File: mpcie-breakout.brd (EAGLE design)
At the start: 70 x 70 mm, 43 parts, among them K1 694108106102, U1 IP4234CZ6, U2 LD1085D2T33R, X1 MPCIE-JAE, X2 MINI-USB-SHIELD-UX60-MB-5ST

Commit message: gitflow-feature-stash: nanoSIM
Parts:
- removed SIM1: SF7W008S1A-R, SF7W008S1A-SIM:SF7W008S1A-RESTR
- removed X3, X4, X5: (no value), laforge:SMA-F-S-TH
- removed Y3, Y4, Y5: (no value), laforge:HRS_UFL
- added J1: 693043020611, Wurth_Connectors_WR-CRD:693043020611
- moved C8 20.9 mm to (-4.95, 47.1)
- moved C7 14.4 mm to (-13.0, 45.0)
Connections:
- removed net N$13: X3.C, Y3.SIG
- removed net N$14: X4.C, Y4.SIG
- removed net N$7: X5.C, Y5.SIG
- net GND: now also J1.C5, J1.S1, J1.S2, J1.S3, J1.S4, J1.S5, J1.S6; no longer SIM1.5, X3.G1, X3.G2, X3.G3, X3.G4, X4.G1, X4.G2, X4.G3, X4.G4, X5.G1, X5.G2, X5.G3, X5.G4, Y3.GND@1, Y3.GND@2, Y4.GND@1, Y4.GND@2, Y5.GND@1, Y5.GND@2
- net USIM_CLK: now also J1.C3; no longer SIM1.3
- net USIM_DATA: now also J1.C7; no longer SIM1.7
- net USIM_POWER: now also J1.C1; no longer SIM1.1
- net USIM_RESET: now also J1.C2; no longer SIM1.2
- net USIM_VPP: now also J1.C6; no longer SIM1.6
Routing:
- net USIM_VPP: track 34.2 -> 17.7 mm
- net USIM_DATA: track 25.1 -> 10.7 mm
- net USIM_POWER: track 35.2 -> 21.4 mm
- net N$14: track 5.61 -> 0.00 mm
- net N$13: track 5.61 -> 0.00 mm
- net N$7: track 5.36 -> 0.00 mm
- net USIM_RESET: track 36.1 -> 37.3 mm
- net USIM_CLK: track 31.5 -> 32.7 mm
- net GND: vias 164 -> 155

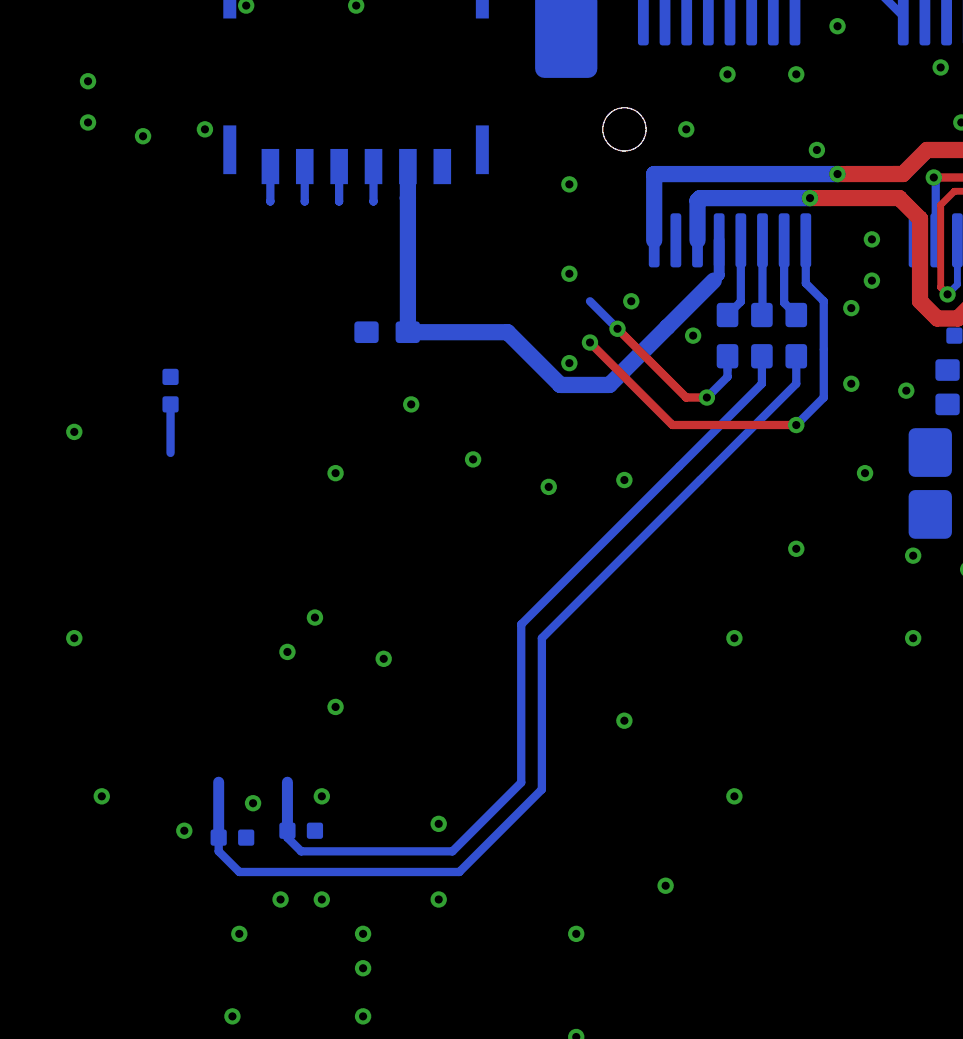
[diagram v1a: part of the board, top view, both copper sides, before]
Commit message: Nano Sim placed.
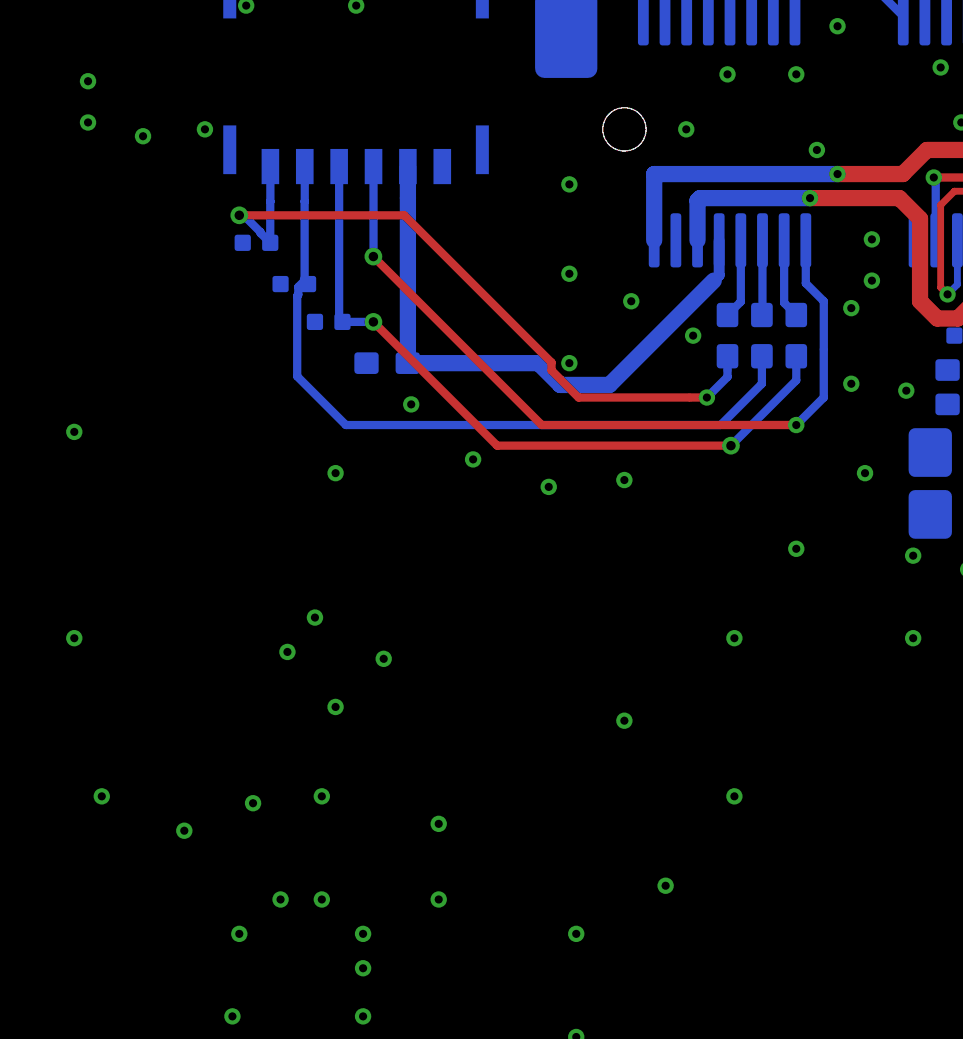
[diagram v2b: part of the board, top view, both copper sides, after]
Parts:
- moved C5 20.2 mm to (-8.38, 48.9), turned to 0 degrees
- moved C6 19.4 mm to (-7.11, 47.5), turned to 0 degrees
- moved C7 6.32 mm to (-9.78, 50.4), turned to 0 degrees
- moved C8 1.14 mm to (-4.95, 46.0)
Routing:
- net USIM_DATA: track 10.7 -> 26.5 mm
- net USIM_VPP: track 17.7 -> 29.0 mm
- net USIM_RESET: track 37.3 -> 26.3 mm, vias 0 -> 2
- net USIM_CLK: track 32.7 -> 27.6 mm
- net USIM_POWER: track 21.4 -> 22.1 mm
